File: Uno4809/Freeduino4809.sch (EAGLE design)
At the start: 58 parts, among them J101 -, U1 ATMEGA4809, Y1 32768Hz

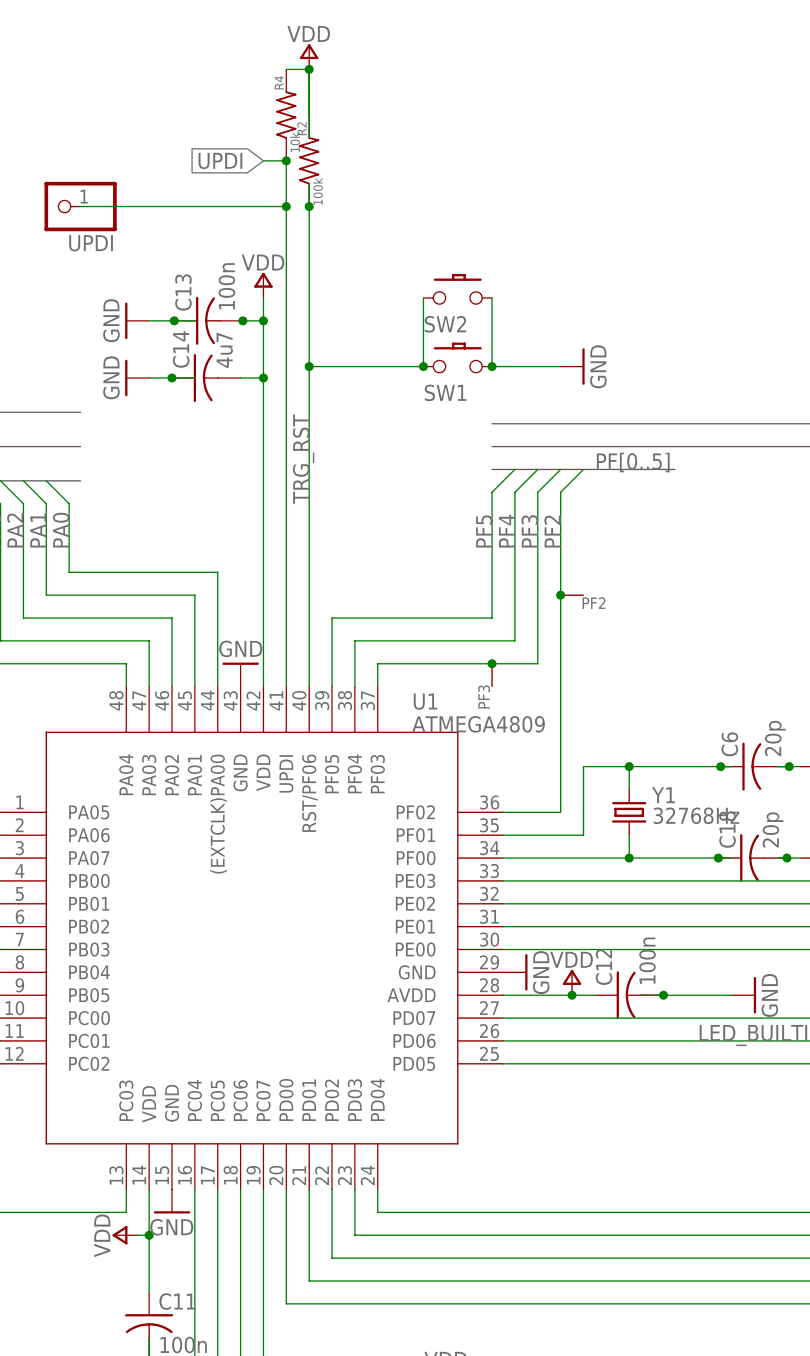
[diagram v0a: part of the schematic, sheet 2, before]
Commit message: Version 0.4 fix RX/TX, move UPDI pin
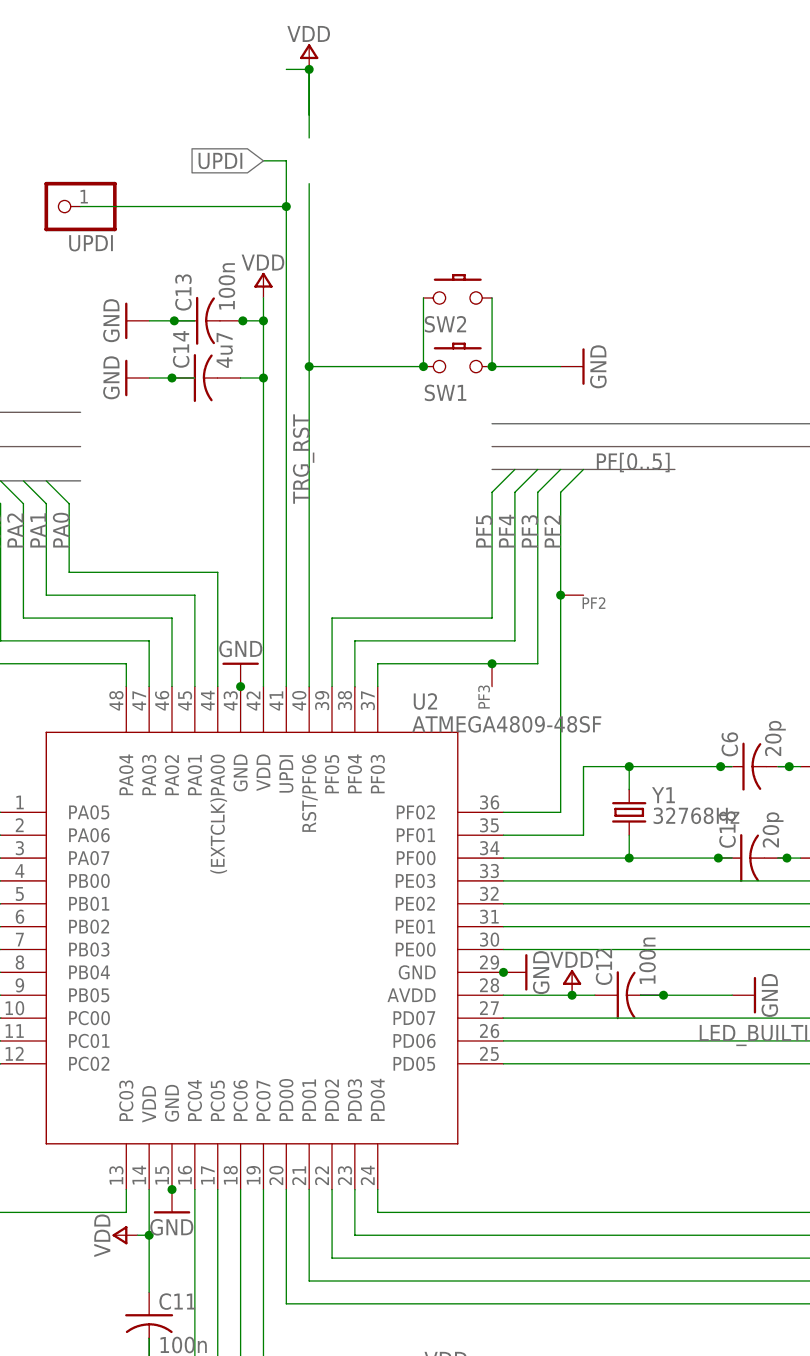
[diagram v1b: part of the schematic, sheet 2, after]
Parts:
- removed R2: 100k, my-rcl:R-US_R0805
- removed R4: 10k, my-rcl:R-US_R0805
- removed U1: ATMEGA4809, Arduino-ucs&SoCs:ATMEGA4809
- added U2: ATMEGA4809-48SF, avr:ATMEGA4809-48SF
- added W1, W2, W3, W4: WIRE-R6, mylib4:WIRE-R6
- VERSION: value 0.3 -> 0.5
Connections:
- net DBG_RX: now also U2.PB04, USBMOD.RXD, W1.P$1, W2.P$1; no longer U1.PB04, USBMOD.TXD
- net DBG_TX: now also U2.PB05, USBMOD.TXD, W3.P$1, W4.P$1; no longer U1.PB05, USBMOD.RXD
- net GND: now also U2.GND@1, U2.GND@2, U2.GND@3; no longer U1.GND@1, U1.GND@2, U1.GND@3
- net LED_BUILTIN: now also U2.PD06; no longer U1.PD06
- net N$4: now also U2.PF00; no longer U1.PF00
- net N$5: now also U2.PF01; no longer U1.PF01
- net PA0: now also U2.(EXTCLK)PA00; no longer U1.(EXTCLK)PA00
- net PA1: now also U2.PA01; no longer U1.PA01
- net PA2: now also U2.PA02; no longer U1.PA02
- net PA3: now also U2.PA03; no longer U1.PA03
- net PA4: now also U2.PA04; no longer U1.PA04
- net PA5: now also U2.PA05; no longer U1.PA05
- net PA6: now also U2.PA06; no longer U1.PA06
- net PA7: now also U2.PA07; no longer U1.PA07
- net PB0: now also U2.PB00; no longer U1.PB00
- net PB1: now also U2.PB01; no longer U1.PB01
- net PB2: now also U2.PB02; no longer U1.PB02
- net PB3: now also U2.PB03; no longer U1.PB03
- net PC0: now also U2.PC00; no longer U1.PC00
- net PC1: now also U2.PC01; no longer U1.PC01
- net PC2: now also U2.PC02; no longer U1.PC02
- net PC3: now also U2.PC03; no longer U1.PC03
- net PC4: now also U2.PC04; no longer U1.PC04
- net PC5: now also U2.PC05; no longer U1.PC05
- net PC6: now also U2.PC06; no longer U1.PC06
- net PC7: now also U2.PC07; no longer U1.PC07
- net PD0: now also U2.PD00; no longer U1.PD00
- net PD1: now also U2.PD01; no longer U1.PD01
- net PD2: now also U2.PD02; no longer U1.PD02
- net PD3: now also U2.PD03; no longer U1.PD03
- net PD4: now also U2.PD04; no longer U1.PD04
- net PD5: now also U2.PD05; no longer U1.PD05
- net PD7: now also U2.PD07; no longer U1.PD07
- net PE0: now also U2.PE00; no longer U1.PE00
- net PE1: now also U2.PE01; no longer U1.PE01
- net PE2: now also U2.PE02; no longer U1.PE02
- net PE3: now also U2.PE03; no longer U1.PE03
- net PF2: now also U2.PF02; no longer U1.PF02
- net PF3: now also U2.PF03; no longer U1.PF03
- net PF4: now also U2.PF04; no longer U1.PF04
- net PF5: now also U2.PF05; no longer U1.PF05
- net TRG_RST: now also U2.RST/PF06; no longer R2.1, U1.RST/PF06
- net UPDI: now also U2.UPDI; no longer R4.1, U1.UPDI
- net VDD: now also U2.AVDD, U2.VDD@1, U2.VDD@2; no longer R2.2, R4.2, U1.AVDD, U1.VDD@1, U1.VDD@2
